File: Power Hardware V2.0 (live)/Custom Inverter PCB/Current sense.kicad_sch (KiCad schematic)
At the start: 49 parts, among them U4 TLV9004IPWR

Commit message: switches instead of relays. Short on half bridge fixed. encoder page made. root page connections fixed
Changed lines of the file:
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@@
-		)
-	)
-	(label "SEN_100V"
-		(at 132.08 158.75 180)
-		(fields_autoplaced yes)
-		(effects
-			(font
-				(size 1.27 1.27)
-			)
-			(justify right bottom)
 		)
 	)
@@
 		(fields_autoplaced yes)
 		(effects
-			(font
-				(size 1.27 1.27)
-			)
-			(justify left)
-		)
-	)
-	(hierarchical_label "SEN_100V"
-		(shape input)
-		(at 132.08 158.75 0)
-		(fields_autoplaced yes)
-		(effects

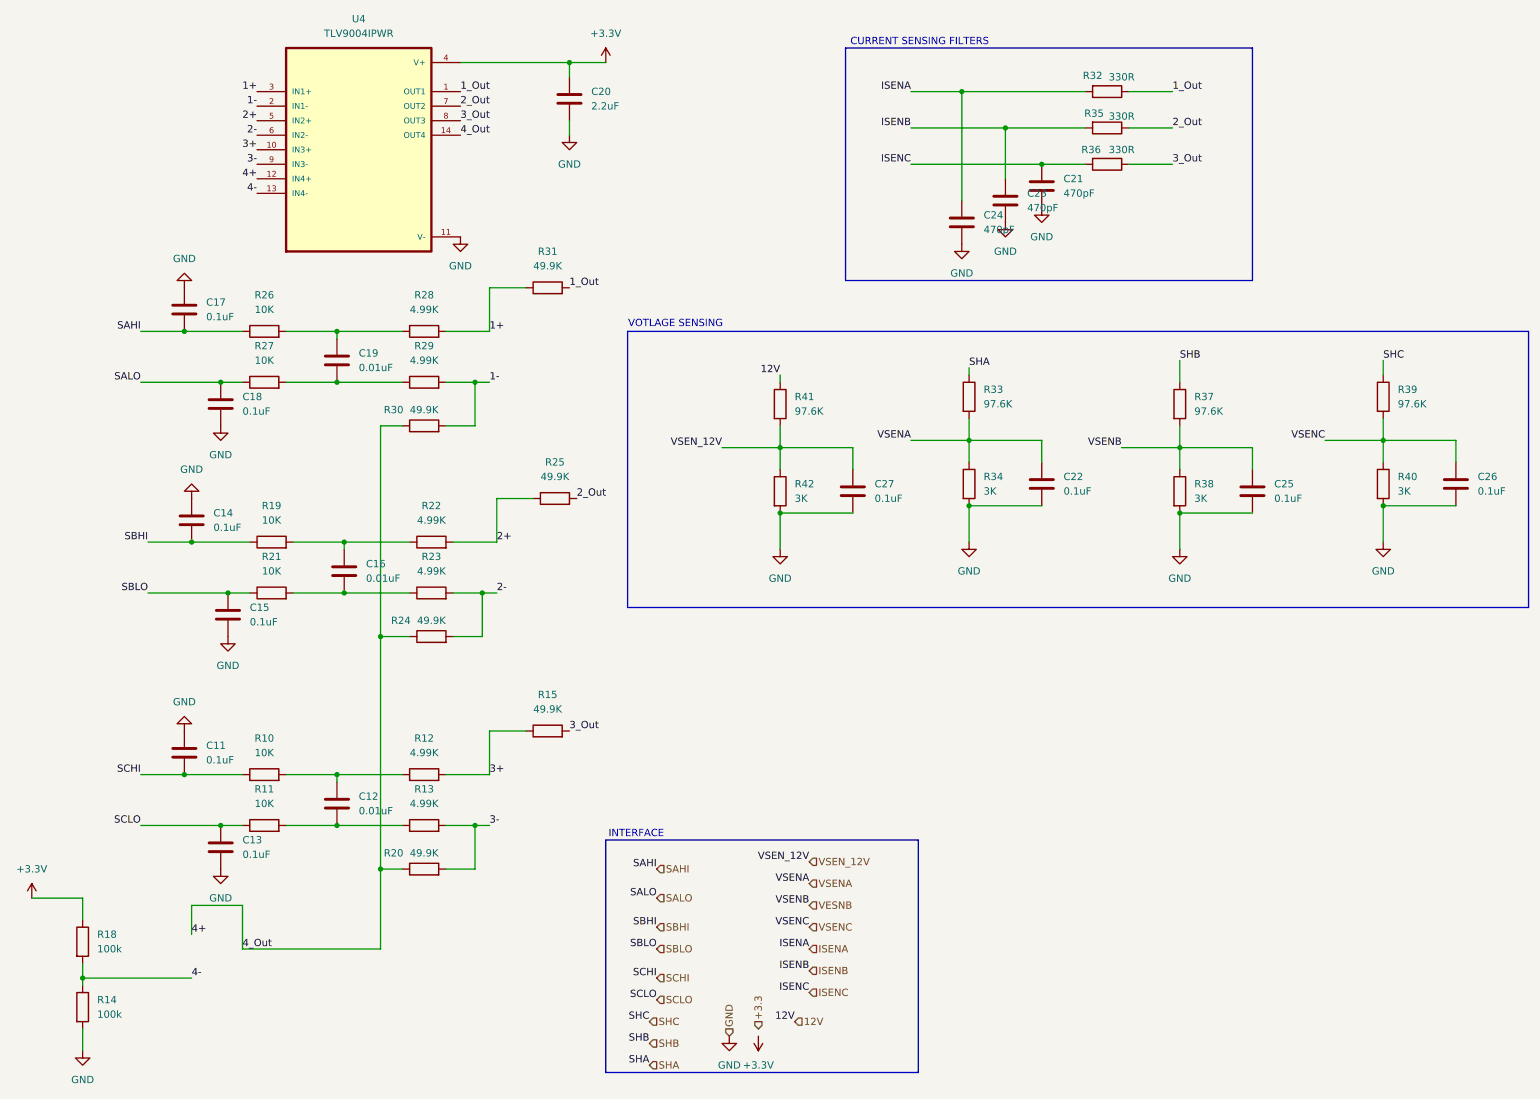
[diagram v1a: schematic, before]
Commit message: Schematic Changes
-Changed 3.3V regulator to a higher power unit for the sin-cos circuit (from 500mA to 3A)
-Fixed flipped MOTA,B,C connection to Output Terminal
- Current Sense IC setup
- Fuses for Phase current outputs
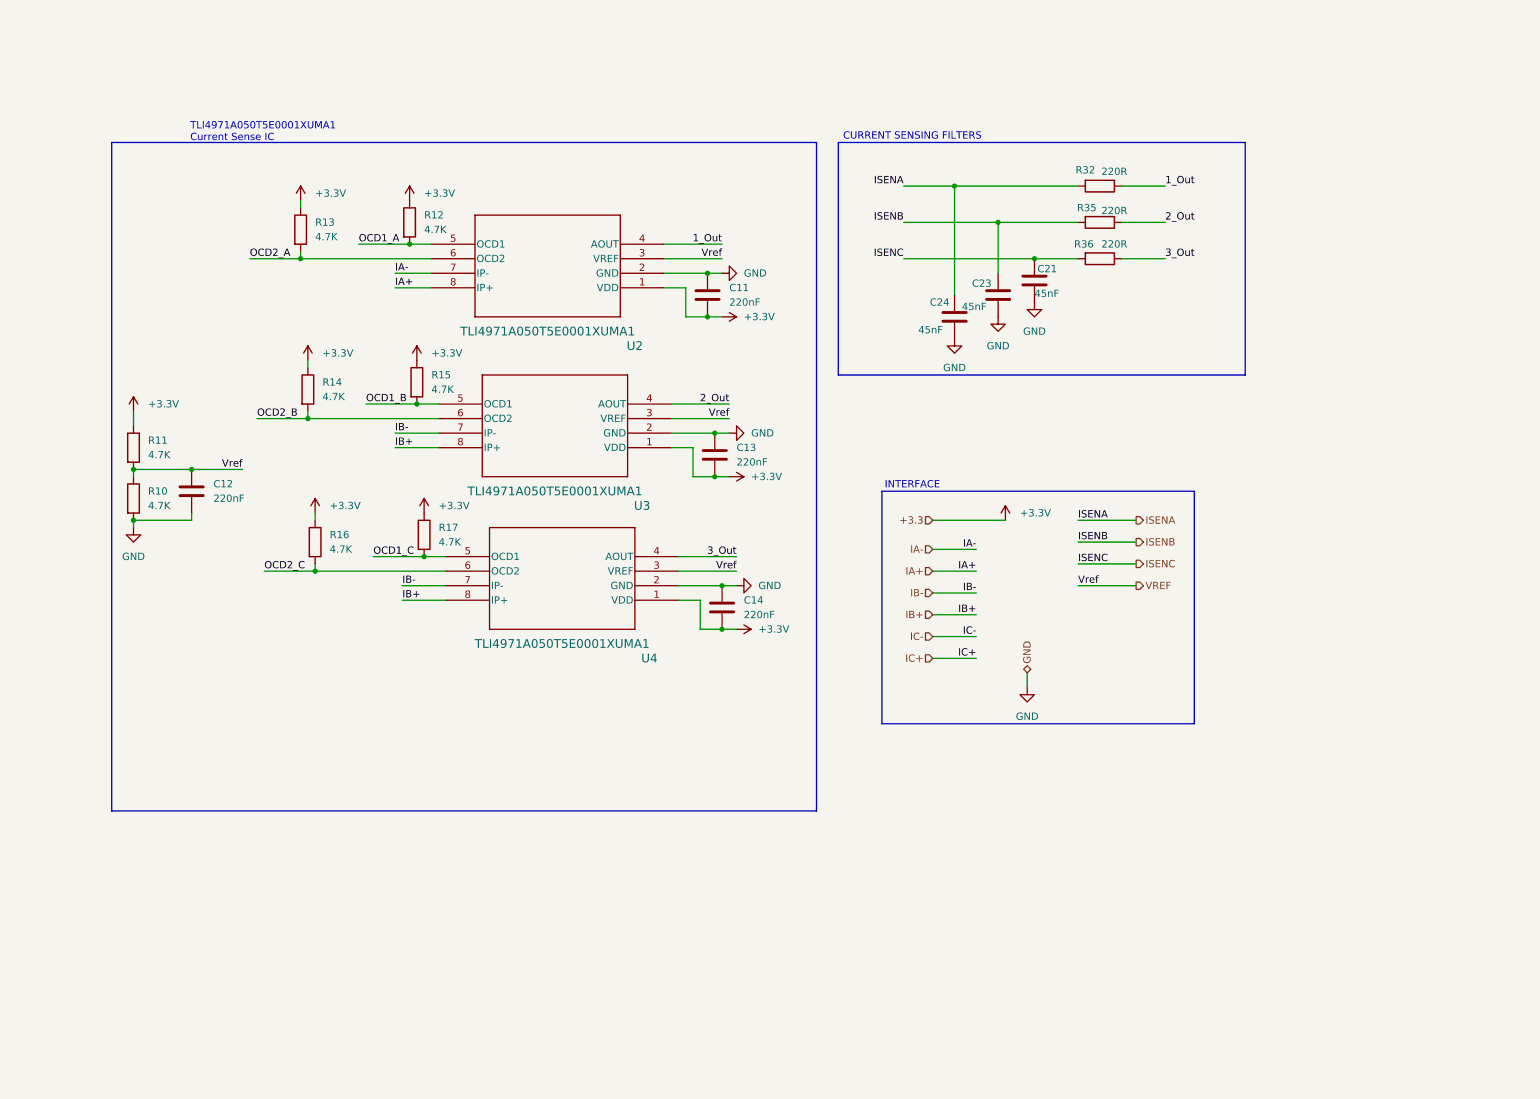
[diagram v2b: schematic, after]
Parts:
- removed C15, C17, C18, C22, C25, C26, C27: 0.1uF, Capacitor_SMD:C_0805_2012Metric, symbol Device:C
- removed C16, C19: 0.01uF, Capacitor_SMD:C_0805_2012Metric, symbol Device:C
- removed C20: 2.2uF, Capacitor_SMD:C_0805_2012Metric, symbol Device:C
- removed R18: 100k, Resistor_SMD:R_0805_2012Metric, symbol Device:R
- removed R19, R21, R26, R27: 10K, Resistor_SMD:R_0805_2012Metric, symbol Device:R
- removed R20, R24, R25, R30, R31: 49.9K, Resistor_SMD:R_0805_2012Metric, symbol Device:R
- removed R22, R23, R28, R29: 4.99K, Resistor_SMD:R_0805_2012Metric, symbol Device:R
- removed R33, R37, R39, R41: 97.6K, Resistor_SMD:R_0805_2012Metric, symbol Device:R
- removed R34, R38, R40, R42: 3K, Resistor_SMD:R_0805_2012Metric, symbol Device:R
- removed U4: TLV9004IPWR, TLV9004IPWR:SOP65P640X120-14N, symbol TLV9004IPWR:TLV9004IPWR
- added R16, R17: 4.7K, Capacitor_SMD:C_0603_1608Metric_Pad1.08x0.95mm_HandSolder, symbol Device:R
- added U2, U3, U4: TLI4971A050T5E0001XUMA1, Current Sense IC TLI4971A:PG-TISON-8-5, symbol Current Sense TLI4971A:TLI4971A120T5UE0001XUMA1
- C11, C13, C14: value 0.1uF -> 220nF; footprint Capacitor_SMD:C_0805_2012Metric -> Capacitor_SMD:C_0603_1608Metric_Pad1.08x0.95mm_HandSolder; Part Number CC0805KRX7R9BB104 -> (none)
- C12: value 0.01uF -> 220nF; footprint Capacitor_SMD:C_0805_2012Metric -> Capacitor_SMD:C_0603_1608Metric_Pad1.08x0.95mm_HandSolder; Part Number KGM21NR71H103KT -> (none)
- C21, C23, C24: value 470pF -> 45nF; Part Number C0805C471K5RACTU -> (none)
- R10, R11: value 10K -> 4.7K; footprint Resistor_SMD:R_0805_2012Metric -> Capacitor_SMD:C_0603_1608Metric_Pad1.08x0.95mm_HandSolder; Part Number RR1220P-103-D -> (none)
- R12, R13: value 4.99K -> 4.7K; footprint Resistor_SMD:R_0805_2012Metric -> Capacitor_SMD:C_0603_1608Metric_Pad1.08x0.95mm_HandSolder; Part Number RG2012P-4991-B-T5 -> (none)
- R14: value 100k -> 4.7K; footprint Resistor_SMD:R_0805_2012Metric -> Capacitor_SMD:C_0603_1608Metric_Pad1.08x0.95mm_HandSolder; Part Number RC0805FR-07100KL -> (none)
- R15: value 49.9K -> 4.7K; footprint Resistor_SMD:R_0805_2012Metric -> Capacitor_SMD:C_0603_1608Metric_Pad1.08x0.95mm_HandSolder; Part Number TNPW080549K9BEEA -> (none)
- R32, R35, R36: value 330R -> 220R; Part Number CR0805-JW-331ELF -> (none)
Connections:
- net 4- is gone; now on net +3.3V: R14.1
- net SBHI is gone; now on net +3.3V: C14.2
- net +3.3V: now also C11.2, C13.2, R11.1, R12.1, R13.1, R15.1, R16.1, R17.1, U2.1 (VDD), U3.1 (VDD), U4.1 (VDD)
- net 1_Out: now also U2.4 (AOUT)
- net 2_Out: now also U3.4 (AOUT)
- net 3_Out: now also U4.4 (AOUT); no longer R15.2
- net GND: now also C12.2, C13.1, R10.2, U2.2 (GND), U3.2 (GND), U4.2 (GND); no longer C13.2, R14.2
- net 3+ renamed OCD1_A
- net OCD1_A: now also U2.5 (OCD1); no longer R15.1
- net 3- renamed OCD2_A
- net OCD2_A: now also U2.6 (OCD2)
- net SCHI renamed VREF
- net VREF: now also C12.1, R11.2, U2.3 (VREF), U3.3 (VREF), U4.3 (VREF); no longer C11.2
- removed net SCLO: C13.1, R11.1
- new net IA+: U2.8 (IP+)
- new net IA-: U2.7 (IP-)
- new net IB+: U3.8 (IP+), U4.8 (IP+)
- new net IB-: U3.7 (IP-), U4.7 (IP-)
- new net OCD1_B: R15.2, U3.5 (OCD1)
- new net OCD1_C: R17.2, U4.5 (OCD1)
- new net OCD2_B: R14.2, U3.6 (OCD2)
- new net OCD2_C: R16.2, U4.6 (OCD2)
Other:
- note added: "TLI4971A050T5E0001XUMA1 Current Sense IC"
- note removed: "VOTLAGE SENSING"
- moved on the sheet: C21, C23, C24, R32, R35, R36

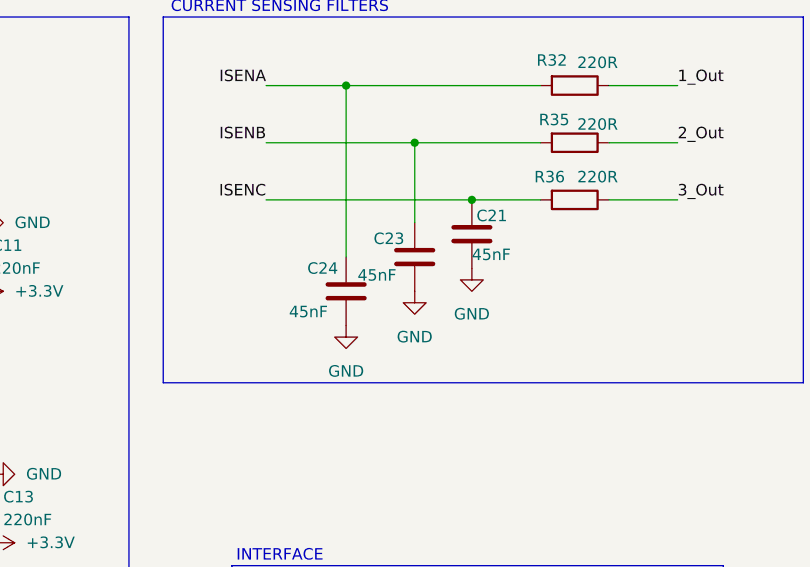
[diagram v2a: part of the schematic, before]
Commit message: Updated parts numbers for current sensing
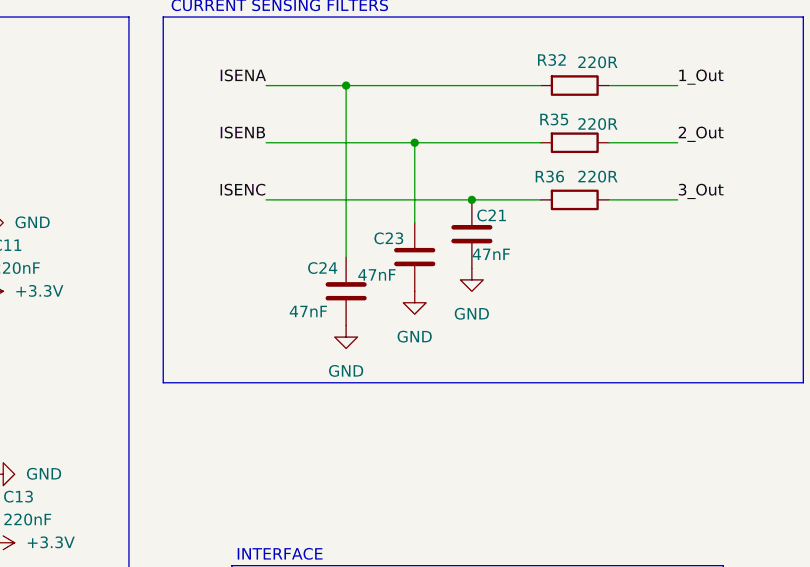
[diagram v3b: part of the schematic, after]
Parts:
- C11, C13, C14: Part Number (none) -> CL21B224KAFNNNE
- C21, C23, C24: value 45nF -> 47nF; Part Number (none) -> C0805C473K5RACTU
- R10, R11, R12, R14, R15, R16, R17: footprint Capacitor_SMD:C_0603_1608Metric_Pad1.08x0.95mm_HandSolder -> Resistor_SMD:R_0805_2012Metric; Part Number (none) -> CRCW08054K70FKEAC
- R13: Part Number (none) -> CRCW08054K70FKEAC
- R32, R35, R36: Part Number (none) -> CRGCQ0805F220R
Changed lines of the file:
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@@
 			)
 		)
-		(property "Footprint" "Capacitor_SMD:C_0603_1608Metric_Pad1.08x0.95mm_HandSolder"
+		(property "Footprint" "Resistor_SMD:R_0805_2012Metric"
 			(at 84.582 48.26 90)
 			(effects
@@
 			)
 		)
-		(property "Part Number" ""
+		(property "Part Number" "CRCW08054K70FKEAC"
 			(at 86.36 48.26 0)
 			(effects
@@
 			)
 		)
-		(property "Value" "45nF"
+		(property "Value" "47nF"
 			(at 175.26 67.056 0)
 			(effects
@@
 			)
 		)
-		(property "Part Number" ""
+		(property "Part Number" "C0805C473K5RACTU"
 			(at 181.61 64.77 0)
 			(effects
@@
 			)
 		)
-		(property "Footprint" "Capacitor_SMD:C_0603_1608Metric_Pad1.08x0.95mm_HandSolder"
+		(property "Footprint" "Resistor_SMD:R_0805_2012Metric"
 			(at 87.122 102.87 90)
 			(effects
@@
 			)
 		)
-		(property "Part Number" ""
+		(property "Part Number" "CRCW08054K70FKEAC"
 			(at 88.9 102.87 0)
 			(effects
@@
 			)
 		)
-		(property "Footprint" "Capacitor_SMD:C_0603_1608Metric_Pad1.08x0.95mm_HandSolder"
+		(property "Footprint" "Resistor_SMD:R_0805_2012Metric"
 			(at 36.322 87.63 90)
 			(effects
@@
 			)
 		)
-		(property "Part Number" ""
+		(property "Part Number" "CRCW08054K70FKEAC"
 			(at 38.1 87.63 0)
 			(effects
@@
 			)
 		)
-		(property "Footprint" "Capacitor_SMD:C_0603_1608Metric_Pad1.08x0.95mm_HandSolder"
+		(property "Footprint" "Resistor_SMD:R_0805_2012Metric"
 			(at 68.072 104.14 90)
 			(effects
@@
 			)
 		)
-		(property "Part Number" ""
+		(property "Part Number" "CRCW08054K70FKEAC"
 			(at 69.85 104.14 0)
 			(effects
@@
 			)
 		)
-		(property "Part Number" ""
+		(property "Part Number" "CL21B224KAFNNNE"
 			(at 139.7 88.9 0)
 			(effects
@@
 			)
 		)
-		(property "Part Number" ""
+		(property "Part Number" "CRGCQ0805F220R"
 			(at 207.01 41.91 0)
 			(effects
@@
 			)
 		)
-		(property "Footprint" "Capacitor_SMD:C_0603_1608Metric_Pad1.08x0.95mm_HandSolder"
+		(property "Footprint" "Resistor_SMD:R_0805_2012Metric"
 			(at 85.852 76.2 90)
 			(effects
@@
 			)
 		)
-		(property "Part Number" ""
+		(property "Part Number" "CRCW08054K70FKEAC"
 			(at 87.63 76.2 0)
 			(effects
@@
 			)
 		)
-		(property "Value" "45nF"
+		(property "Value" "47nF"
 			(at 195.58 60.706 0)
 			(effects
@@
 			)
 		)
-		(property "Part Number" ""
+		(property "Part Number" "C0805C473K5RACTU"
 			(at 195.58 58.42 0)
 			(effects
@@
 			)
 		)
-		(property "Value" "45nF"
+		(property "Value" "47nF"
 			(at 182.88 62.992 0)
 			(effects
@@
 			)
 		)
-		(property "Part Number" ""
+		(property "Part Number" "C0805C473K5RACTU"
 			(at 189.23 60.96 0)
 			(effects
@@
 			)
 		)
-		(property "Part Number" ""
+		(property "Part Number" "CL21B224KAFNNNE"
 			(at 140.97 115.57 0)
 			(effects
@@
 			)
 		)
-		(property "Part Number" ""
+		(property "Part Number" "CRGCQ0805F220R"
 			(at 207.01 48.26 0)
 			(effects
@@
 			)
 		)
-		(property "Footprint" "Capacitor_SMD:C_0603_1608Metric_Pad1.08x0.95mm_HandSolder"
+		(property "Footprint" "Resistor_SMD:R_0805_2012Metric"
 			(at 66.802 77.47 90)
 			(effects
@@
 			)
 		)
-		(property "Part Number" ""
+		(property "Part Number" "CRCW08054K70FKEAC"
 			(at 68.58 77.47 0)
 			(effects
@@
 			)
 		)
-		(property "Part Number" ""
+		(property "Part Number" "CRGCQ0805F220R"
 			(at 207.01 54.61 0)
 			(effects
@@
 			)
 		)
-		(property "Footprint" "Capacitor_SMD:C_0603_1608Metric_Pad1.08x0.95mm_HandSolder"
+		(property "Footprint" "Resistor_SMD:R_0805_2012Metric"
 			(at 36.322 96.52 90)
 			(effects
@@
 			)
 		)
-		(property "Part Number" ""
+		(property "Part Number" "CRCW08054K70FKEAC"
 			(at 38.1 96.52 0)
 			(effects
@@
 			)
 		)
-		(property "Part Number" ""
+		(property "Part Number" "CRCW08054K70FKEAC"
 			(at 67.31 49.53 0)
 			(effects
@@
 			)
 		)
-		(property "Part Number" ""
+		(property "Part Number" "CL21B224KAFNNNE"
 			(at 138.43 60.96 0)
 			(effects

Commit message: no changes
no
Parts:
- C12: Part Number (none) -> CL21B224KAFNNNE
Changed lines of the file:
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@@
 			)
 		)
-		(property "Part Number" ""
+		(property "Part Number" "CL21B224KAFNNNE"
 			(at 48.26 95.25 0)
 			(effects

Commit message: no major changes
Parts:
- U2, U3, U4: footprint Current Sense IC TLI4971A:PG-TISON-8-5 -> TLI4971A:PG-TISON-8-5
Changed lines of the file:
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@@
 			)
 		)
-		(property "Footprint" "Current Sense IC TLI4971A:PG-TISON-8-5"
+		(property "Footprint" "TLI4971A:PG-TISON-8-5"
 			(at 130.81 59.69 0)
 			(effects
@@
 			)
 		)
-		(property "Footprint" "Current Sense IC TLI4971A:PG-TISON-8-5"
+		(property "Footprint" "TLI4971A:PG-TISON-8-5"
 			(at 132.08 87.63 0)
 			(effects
@@
 			)
 		)
-		(property "Footprint" "Current Sense IC TLI4971A:PG-TISON-8-5"
+		(property "Footprint" "TLI4971A:PG-TISON-8-5"
 			(at 133.35 114.3 0)
 			(effects

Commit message: footprint fixes
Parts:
- C11, C12, C13, C14: footprint Capacitor_SMD:C_0603_1608Metric_Pad1.08x0.95mm_HandSolder -> Capacitor_SMD:C_0603_1608Metric
- R13: footprint Capacitor_SMD:C_0603_1608Metric_Pad1.08x0.95mm_HandSolder -> Resistor_SMD:R_0805_2012Metric
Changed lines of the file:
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@@
 			)
 		)
-		(property "Footprint" "Capacitor_SMD:C_0603_1608Metric_Pad1.08x0.95mm_HandSolder"
+		(property "Footprint" "Capacitor_SMD:C_0603_1608Metric"
 			(at 140.6652 92.71 0)
 			(effects
@@
 			)
 		)
-		(property "Footprint" "Capacitor_SMD:C_0603_1608Metric_Pad1.08x0.95mm_HandSolder"
+		(property "Footprint" "Capacitor_SMD:C_0603_1608Metric"
 			(at 141.9352 119.38 0)
 			(effects
@@
 			)
 		)
-		(property "Footprint" "Capacitor_SMD:C_0603_1608Metric_Pad1.08x0.95mm_HandSolder"
+		(property "Footprint" "Capacitor_SMD:C_0603_1608Metric"
 			(at 49.2252 99.06 0)
 			(effects
@@
 			)
 		)
-		(property "Footprint" "Capacitor_SMD:C_0603_1608Metric_Pad1.08x0.95mm_HandSolder"
+		(property "Footprint" "Resistor_SMD:R_0805_2012Metric"
 			(at 65.532 49.53 90)
 			(effects
@@
 			)
 		)
-		(property "Footprint" "Capacitor_SMD:C_0603_1608Metric_Pad1.08x0.95mm_HandSolder"
+		(property "Footprint" "Capacitor_SMD:C_0603_1608Metric"
 			(at 139.3952 64.77 0)
 			(effects

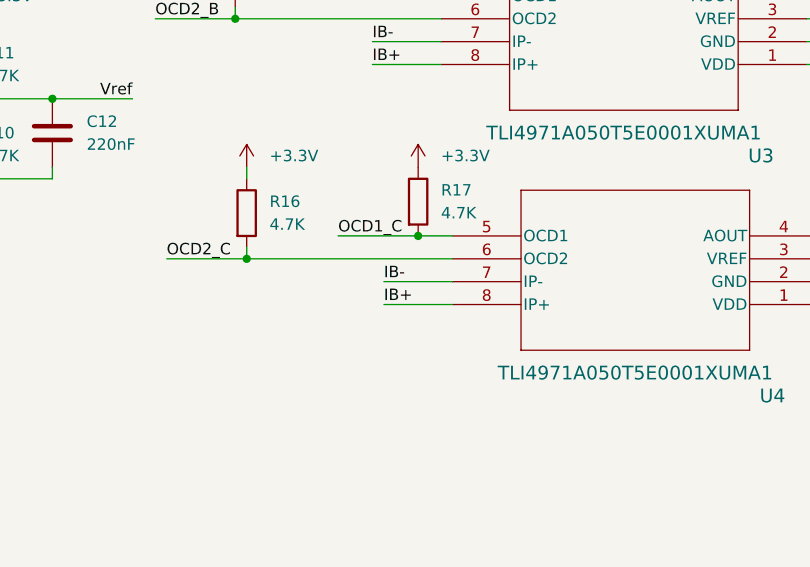
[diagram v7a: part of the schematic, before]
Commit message: Pcb layout and tracing
changed footprint file for current sense ic
did layout and tracing for pcb
created bom
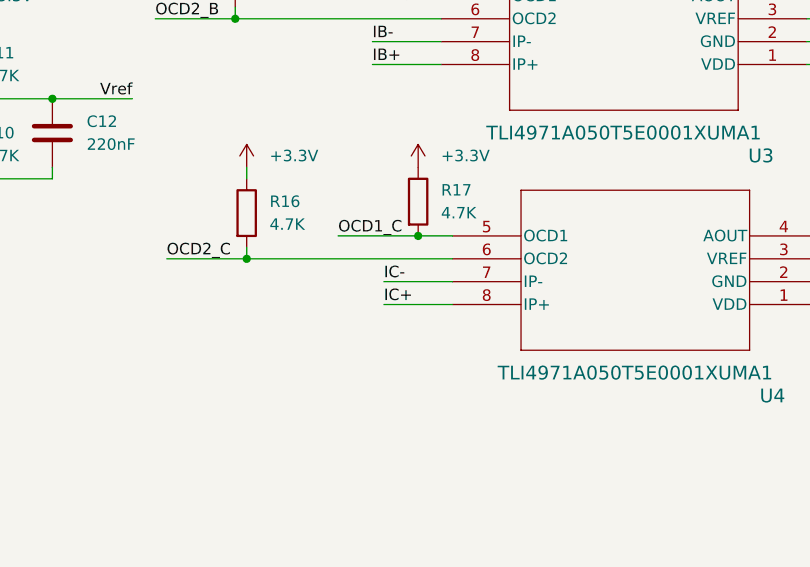
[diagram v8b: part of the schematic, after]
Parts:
- U2, U3, U4: footprint TLI4971A:PG-TISON-8-5 -> TLI4971A:IC_TLI4971A050T5UE0001XUMA1
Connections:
- net IB+: no longer U4.8 (IP+)
- net IB-: no longer U4.7 (IP-)
- net IC+: now also U4.8 (IP+)
- net IC-: now also U4.7 (IP-)
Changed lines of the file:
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@@
 		)
 	)
-	(label "IB+"
+	(label "IC+"
 		(at 85.09 114.3 0)
 		(effects
@@
 		)
 	)
-	(label "IB-"
+	(label "IC-"
 		(at 85.09 111.76 0)
 		(effects
@@
 			)
 		)
-		(property "Footprint" "TLI4971A:PG-TISON-8-5"
+		(property "Footprint" "TLI4971A:IC_TLI4971A050T5UE0001XUMA1"
 			(at 130.81 59.69 0)
 			(effects
@@
 			)
 		)
-		(property "Footprint" "TLI4971A:PG-TISON-8-5"
+		(property "Footprint" "TLI4971A:IC_TLI4971A050T5UE0001XUMA1"
 			(at 132.08 87.63 0)
 			(effects
@@
 			)
 		)
-		(property "Footprint" "TLI4971A:PG-TISON-8-5"
+		(property "Footprint" "TLI4971A:IC_TLI4971A050T5UE0001XUMA1"
 			(at 133.35 114.3 0)
 			(effects
